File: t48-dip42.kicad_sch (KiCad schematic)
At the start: 3 parts, among them J1 EPROM, J2 To T48 socket, J3 To T48 ribbon

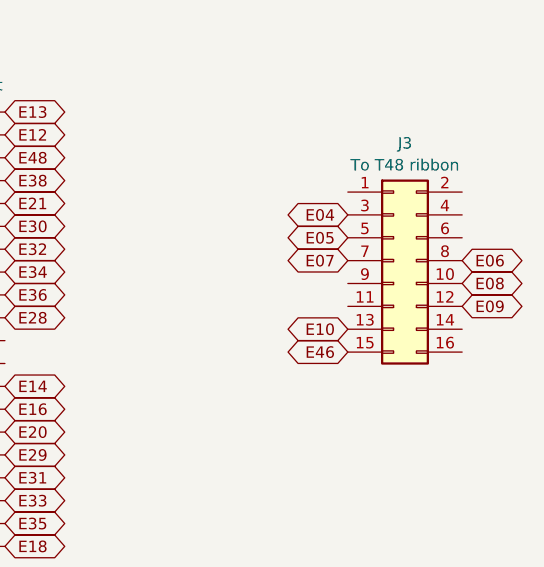
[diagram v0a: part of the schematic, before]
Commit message: v03: Fix swapped upper/lower pins on ribbon cable
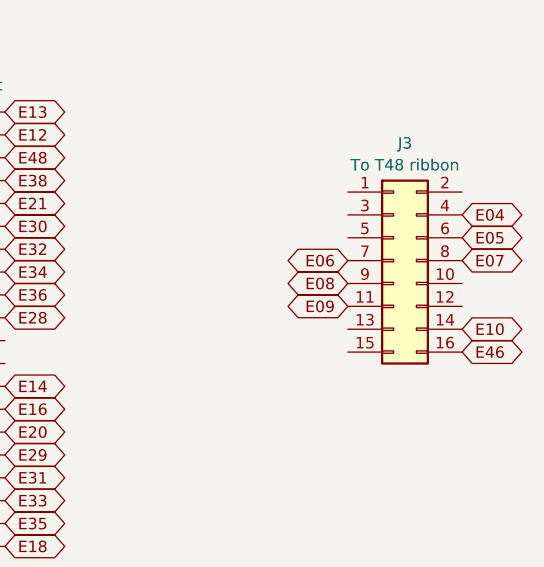
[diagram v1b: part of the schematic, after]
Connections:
- net E04: now also J3.4 (Pin_4); no longer J3.3 (Pin_3)
- net E05: now also J3.6 (Pin_6); no longer J3.5 (Pin_5)
- net E06: now also J3.7 (Pin_7); no longer J3.8 (Pin_8)
- net E07: now also J3.8 (Pin_8); no longer J3.7 (Pin_7)
- net E08: now also J3.9 (Pin_9); no longer J3.10 (Pin_10)
- net E09: now also J3.11 (Pin_11); no longer J3.12 (Pin_12)
- net E10: now also J3.14 (Pin_14); no longer J3.13 (Pin_13)
- net E46: now also J3.16 (Pin_16); no longer J3.15 (Pin_15)
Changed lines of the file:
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@@
     )
   )
-  (global_label "E46" (shape bidirectional) (at 177.8 87.63 180) (fields_autoplaced)
-    (effects (font (size 1.27 1.27)) (justify right))
-    (property "Intersheetrefs" "${INTERSHEET_REFS}" (at 170.1355 87.63 0)
-      (effects (font (size 1.27 1.27)) (justify right) hide)
+  (global_label "E46" (shape bidirectional) (at 190.5 87.63 0) (fields_autoplaced)
+    (effects (font (size 1.27 1.27)) (justify left))
+    (property "Intersheetrefs" "${INTERSHEET_REFS}" (at 198.1645 87.63 0)
+      (effects (font (size 1.27 1.27)) (justify left) hide)
     )
   )
@@
     )
   )
-  (global_label "E10" (shape bidirectional) (at 177.8 85.09 180) (fields_autoplaced)
-    (effects (font (size 1.27 1.27)) (justify right))
-    (property "Intersheetrefs" "${INTERSHEET_REFS}" (at 170.1355 85.09 0)
-      (effects (font (size 1.27 1.27)) (justify right) hide)
+  (global_label "E10" (shape bidirectional) (at 190.5 85.09 0) (fields_autoplaced)
+    (effects (font (size 1.27 1.27)) (justify left))
+    (property "Intersheetrefs" "${INTERSHEET_REFS}" (at 198.1645 85.09 0)
+      (effects (font (size 1.27 1.27)) (justify left) hide)
     )
   )
@@
     )
   )
-  (global_label "E08" (shape bidirectional) (at 190.5 80.01 0) (fields_autoplaced)
-    (effects (font (size 1.27 1.27)) (justify left))
-    (property "Intersheetrefs" "${INTERSHEET_REFS}" (at 198.1645 80.01 0)
-      (effects (font (size 1.27 1.27)) (justify left) hide)
+  (global_label "E08" (shape bidirectional) (at 177.8 80.01 180) (fields_autoplaced)
+    (effects (font (size 1.27 1.27)) (justify right))
+    (property "Intersheetrefs" "${INTERSHEET_REFS}" (at 170.1355 80.01 0)
+      (effects (font (size 1.27 1.27)) (justify right) hide)
     )
   )
@@
     )
   )
-  (global_label "E04" (shape bidirectional) (at 177.8 72.39 180) (fields_autoplaced)
-    (effects (font (size 1.27 1.27)) (justify right))
-    (property "Intersheetrefs" "${INTERSHEET_REFS}" (at 170.1355 72.39 0)
-      (effects (font (size 1.27 1.27)) (justify right) hide)
+  (global_label "E04" (shape bidirectional) (at 190.5 72.39 0) (fields_autoplaced)
+    (effects (font (size 1.27 1.27)) (justify left))
+    (property "Intersheetrefs" "${INTERSHEET_REFS}" (at 198.1645 72.39 0)
+      (effects (font (size 1.27 1.27)) (justify left) hide)
     )
   )
@@
     )
   )
-  (global_label "E09" (shape bidirectional) (at 190.5 82.55 0) (fields_autoplaced)
-    (effects (font (size 1.27 1.27)) (justify left))
-    (property "Intersheetrefs" "${INTERSHEET_REFS}" (at 198.1645 82.55 0)
-      (effects (font (size 1.27 1.27)) (justify left) hide)
+  (global_label "E09" (shape bidirectional) (at 177.8 82.55 180) (fields_autoplaced)
+    (effects (font (size 1.27 1.27)) (justify right))
+    (property "Intersheetrefs" "${INTERSHEET_REFS}" (at 170.1355 82.55 0)
+      (effects (font (size 1.27 1.27)) (justify right) hide)
     )
   )
@@
     )
   )
-  (global_label "E06" (shape bidirectional) (at 190.5 77.47 0) (fields_autoplaced)
+  (global_label "E06" (shape bidirectional) (at 177.8 77.47 180) (fields_autoplaced)
+    (effects (font (size 1.27 1.27)) (justify right))
+    (property "Intersheetrefs" "${INTERSHEET_REFS}" (at 170.1355 77.47 0)
+      (effects (font (size 1.27 1.27)) (justify right) hide)
+    )
+  )
+  (global_label "E44" (shape bidirectional) (at 76.2 66.04 0) (fields_autoplaced)
+    (effects (font (size 1.27 1.27)) (justify left))
+    (property "Intersheetrefs" "${INTERSHEET_REFS}" (at 83.8645 66.04 0)
+      (effects (font (size 1.27 1.27)) (justify left) hide)
+    )
+  )
+  (global_label "E02" (shape bidirectional) (at 63.5 58.42 180) (fields_autoplaced)
+    (effects (font (size 1.27 1.27)) (justify right))
+    (property "Intersheetrefs" "${INTERSHEET_REFS}" (at 55.8355 58.42 0)
+      (effects (font (size 1.27 1.27)) (justify right) hide)
+    )
+  )
+  (global_label "E33" (shape bidirectional) (at 139.7 104.14 0) (fields_autoplaced)
+    (effects (font (size 1.27 1.27)) (justify left))
+    (property "Intersheetrefs" "${INTERSHEET_REFS}" (at 147.3645 104.14 0)
+      (effects (font (size 1.27 1.27)) (justify left) hide)
+    )
+  )
+  (global_label "E44" (shape bidirectional) (at 127 86.36 180) (fields_autoplaced)
+    (effects (font (size 1.27 1.27)) (justify right))
+    (property "Intersheetrefs" "${INTERSHEET_REFS}" (at 119.3355 86.36 0)
+      (effects (font (size 1.27 1.27)) (justify right) hide)
+    )
+  )
+  (global_label "E19" (shape bidirectional) (at 127 109.22 180) (fields_autoplaced)
+    (effects (font (size 1.27 1.27)) (justify right))
+    (property "Intersheetrefs" "${INTERSHEET_REFS}" (at 119.3355 109.22 0)
+      (effects (font (size 1.27 1.27)) (justify right) hide)
+    )
+  )
+  (global_label "E07" (shape bidirectional) (at 190.5 77.47 0) (fields_autoplaced)
     (effects (font (size 1.27 1.27)) (justify left))
     (property "Intersheetrefs" "${INTERSHEET_REFS}" (at 198.1645 77.47 0)
@@
     )
   )
-  (global_label "E44" (shape bidirectional) (at 76.2 66.04 0) (fields_autoplaced)
-    (effects (font (size 1.27 1.27)) (justify left))
-    (property "Intersheetrefs" "${INTERSHEET_REFS}" (at 83.8645 66.04 0)
-      (effects (font (size 1.27 1.27)) (justify left) hide)
-    )
-  )
-  (global_label "E02" (shape bidirectional) (at 63.5 58.42 180) (fields_autoplaced)
-    (effects (font (size 1.27 1.27)) (justify right))
-    (property "Intersheetrefs" "${INTERSHEET_REFS}" (at 55.8355 58.42 0)
-      (effects (font (size 1.27 1.27)) (justify right) hide)
-    )
-  )
-  (global_label "E33" (shape bidirectional) (at 139.7 104.14 0) (fields_autoplaced)
-    (effects (font (size 1.27 1.27)) (justify left))
-    (property "Intersheetrefs" "${INTERSHEET_REFS}" (at 147.3645 104.14 0)
-      (effects (font (size 1.27 1.27)) (justify left) hide)
-    )
-  )
-  (global_label "E44" (shape bidirectional) (at 127 86.36 180) (fields_autoplaced)
-    (effects (font (size 1.27 1.27)) (justify right))
-    (property "Intersheetrefs" "${INTERSHEET_REFS}" (at 119.3355 86.36 0)
-      (effects (font (size 1.27 1.27)) (justify right) hide)
-    )
-  )
-  (global_label "E19" (shape bidirectional) (at 127 109.22 180) (fields_autoplaced)
-    (effects (font (size 1.27 1.27)) (justify right))
-    (property "Intersheetrefs" "${INTERSHEET_REFS}" (at 119.3355 109.22 0)
-      (effects (font (size 1.27 1.27)) (justify right) hide)
-    )
-  )
-  (global_label "E07" (shape bidirectional) (at 177.8 77.47 180) (fields_autoplaced)
-    (effects (font (size 1.27 1.27)) (justify right))
-    (property "Intersheetrefs" "${INTERSHEET_REFS}" (at 170.1355 77.47 0)
-      (effects (font (size 1.27 1.27)) (justify right) hide)
-    )
-  )
   (global_label "E34" (shape bidirectional) (at 139.7 78.74 0) (fields_autoplaced)
     (effects (font (size 1.27 1.27)) (justify left))
@@
     )
   )
-  (global_label "E05" (shape bidirectional) (at 177.8 74.93 180) (fields_autoplaced)
-    (effects (font (size 1.27 1.27)) (justify right))
-    (property "Intersheetrefs" "${INTERSHEET_REFS}" (at 170.1355 74.93 0)
-      (effects (font (size 1.27 1.27)) (justify right) hide)
-    )
-  )
+  (global_label "E05" (shape bidirectional) (at 190.5 74.93 0) (fields_autoplaced)
+    (effects (font (size 1.27 1.27)) (justify left))
+    (property "Intersheetrefs" "${INTERSHEET_REFS}" (at 198.1645 74.93 0)
+      (effects (font (size 1.27 1.27)) (justify left) hide)
+    )
+  )
